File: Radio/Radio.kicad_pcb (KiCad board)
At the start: 2 copper layers, 65 x 125.5 mm, 34 parts, among them IC1 SI4844-A10-GU, J1 AudioJack3, J2 Conn_01x04_Pin, J3 AM_ANTENNA_CONNECTOR, Q1 NPN, U1 ARDUINO_PRO_MINI, Y1 32.768 kHz

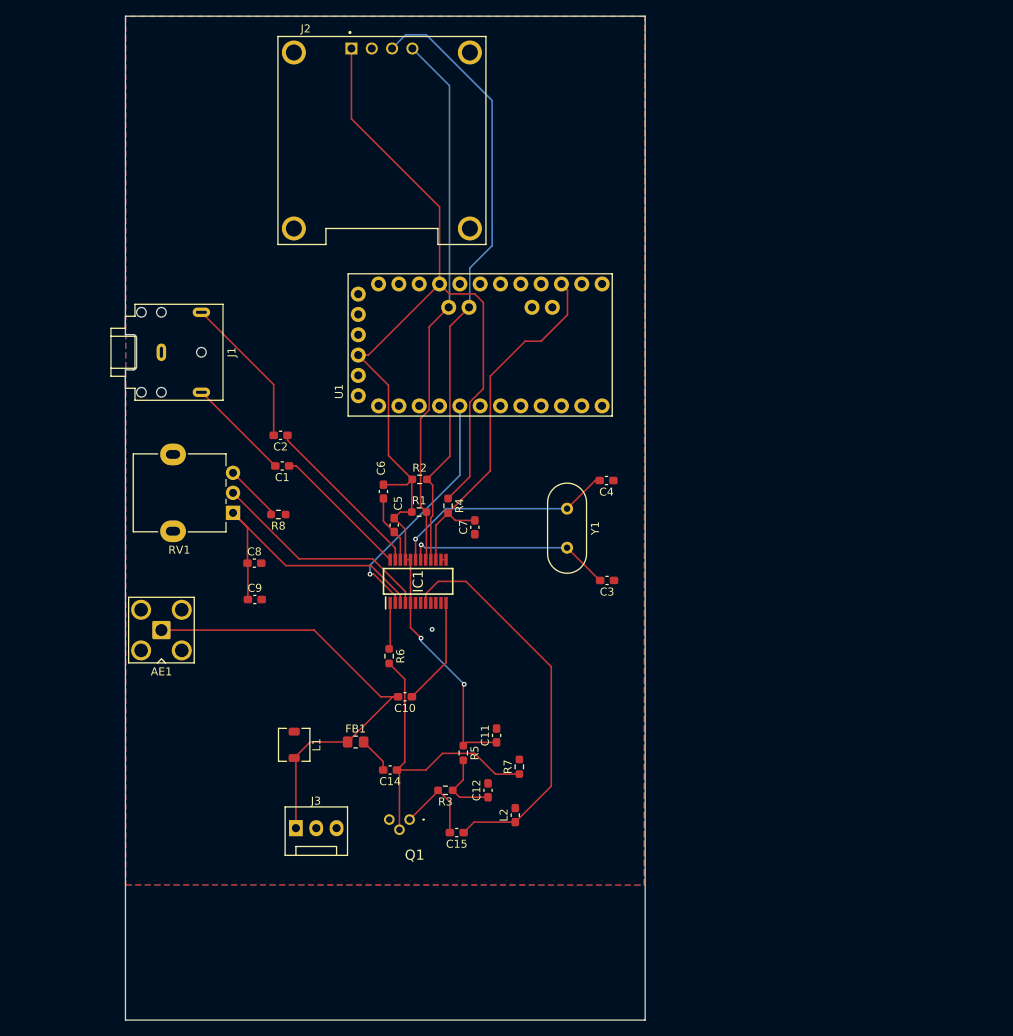
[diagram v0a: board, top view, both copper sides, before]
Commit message: Update PCB: move components
Moved several components to new positions. and changed potentiometer footprint
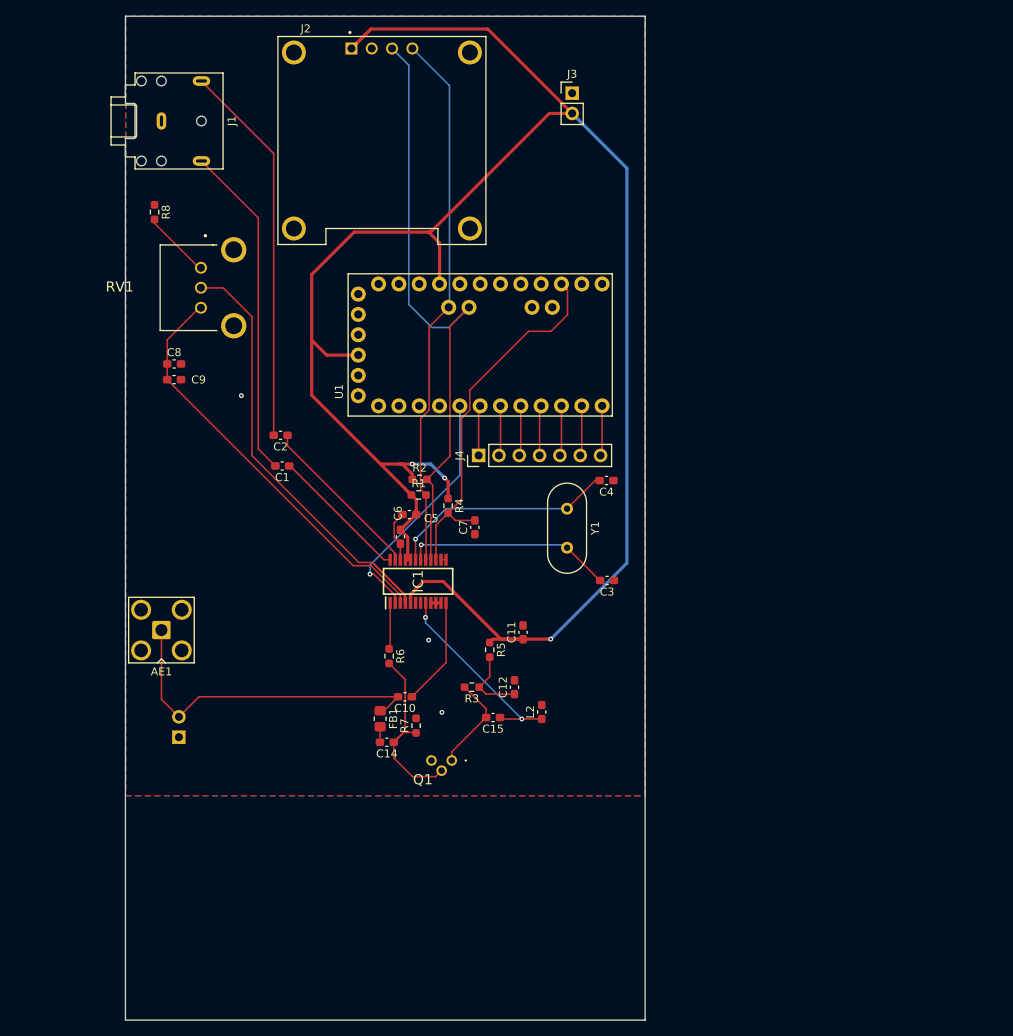
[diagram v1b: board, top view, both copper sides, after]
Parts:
- added J4: Conn_01x07_Pin, Connector_PinHeader_2.54mm:PinHeader_1x07_P2.54mm_Vertical, F.Cu at (115.2, 71.6)
- J3: value AM_ANTENNA_CONNECTOR -> Conn_01x02_Socket; footprint Connector:FanPinHeader_1x03_P2.54mm_Vertical -> Connector_PinHeader_2.54mm:PinHeader_1x02_P2.54mm_Vertical
- L1: value AM_ANT -> L_Ferrite_Small; footprint Inductor_SMD:L_Murata_DEM3518C -> Connector_PinHeader_2.54mm:PinHeader_1x02_P2.54mm_Horizontal; moved to B.Cu
- RV1: footprint Potentiometer_THT:Potentiometer_Alpha_RD901F-40-00D_Single_Vertical -> RadioLib:RK09L1120A2S
- moved J3 98.2 mm to (126.9, 26.4)
- moved R8 40.8 mm to (74.7, 41.2), turned to -90 degrees
- moved RV1 30.9 mm to (80.5, 48.2)
- moved C9 29.3 mm to (77.2, 62.2)
- moved J1 28.9 mm to (75.6, 29.8)
- moved C8 26.8 mm to (77.2, 60.2)
- moved C15 15.1 mm to (117.0, 104.4)
- moved L1 14.4 mm to (77.8, 106.9), turned to 0 degrees
- moved R7 13.9 mm to (107.4, 105.4)
- moved L2 13.3 mm to (123.1, 103.7)
- moved R3 13.3 mm to (114.4, 100.6)
- moved C11 13.3 mm to (120.8, 93.8)
- moved C12 13.3 mm to (119.7, 100.6)
- moved R5 13.3 mm to (116.6, 95.9)
- moved Q1 9.07 mm to (111.9, 109.8)
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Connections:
- J3 pad 1: AM_ANT -> GND
- J3 pad 2: GND -> +3V3
- RV1 pad 1: TUNE1 -> Net-(R8-Pad2)
- RV1 pad 3: Net-(R8-Pad2) -> TUNE1
- U1 pad JP7_1: unconnected-(U1-D9-PadJP7_1) -> ROW1
- U1 pad JP7_2: unconnected-(U1-D8-PadJP7_2) -> ROW2
- U1 pad JP7_3: unconnected-(U1-D7-PadJP7_3) -> ROW3
- U1 pad JP7_4: unconnected-(U1-D6-PadJP7_4) -> ROW4
- U1 pad JP7_5: unconnected-(U1-D5-PadJP7_5) -> COL1
- U1 pad JP7_6: unconnected-(U1-D4-PadJP7_6) -> COL2
- U1 pad JP7_7: unconnected-(U1-D3-PadJP7_7) -> COL3
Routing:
- net +3V3: track 146.3 -> 249.1 mm, vias 2 -> 3
- net TUNE2: track 28.1 -> 59.7 mm
- net Net-(C1-Pad2): track 13.1 -> 42.5 mm
- net Net-(C2-Pad2): track 19.1 -> 48.0 mm
- net FM_ANT: track 50.2 -> 24.8 mm, vias 0 -> 2
- net Net-(Q1-B): track 39.4 -> 23.8 mm
- net AM_ANT: track 58.1 -> 43.6 mm
- net TUNE1: track 38.0 -> 51.9 mm
- net ROW3: track 0.00 -> 6.28 mm
- net COL3: track 0.00 -> 6.28 mm
- net COL1: track 0.00 -> 6.28 mm
- net ROW4: track 0.00 -> 6.28 mm
- net ROW2: track 0.00 -> 6.28 mm
- net COL2: track 0.00 -> 6.28 mm
- net ROW1: track 0.00 -> 6.28 mm
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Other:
- outline, holes or cut-outs redrawn

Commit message: Update PCB layout and footprints
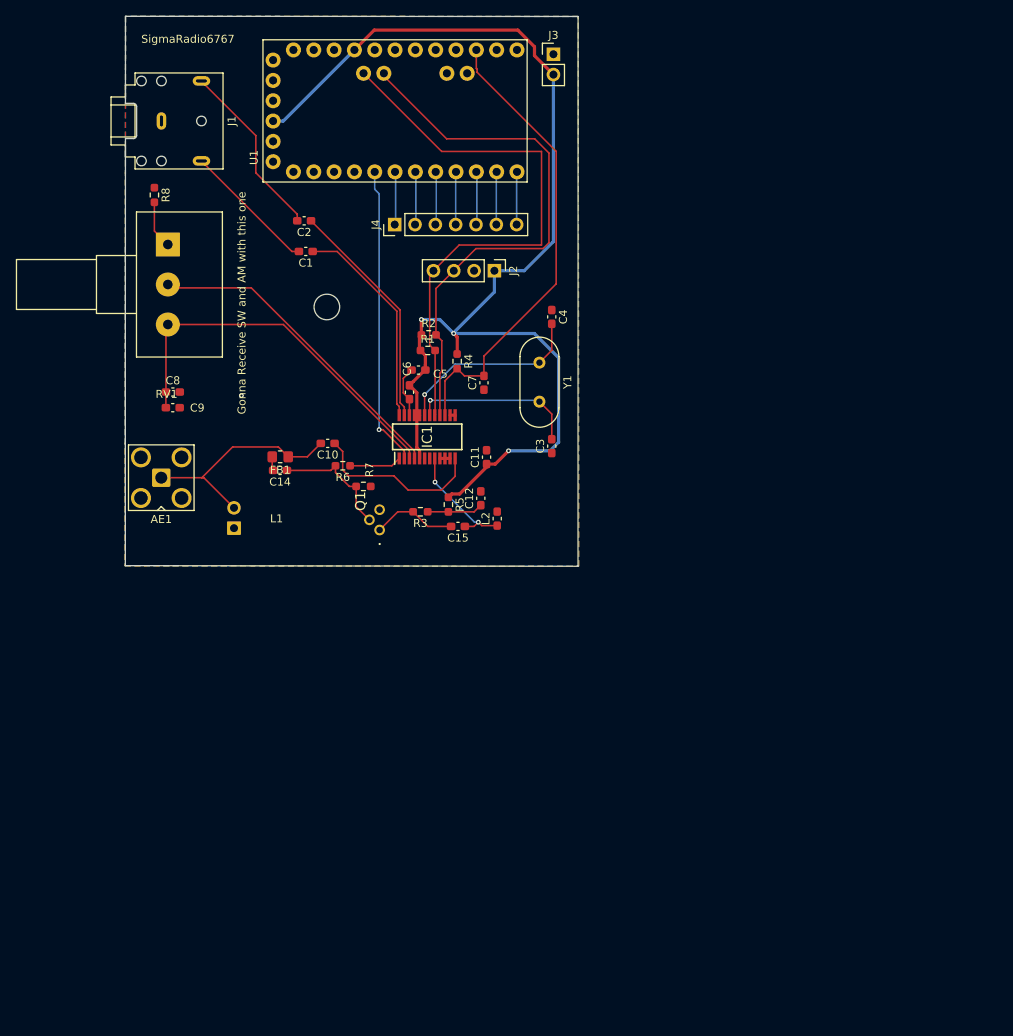
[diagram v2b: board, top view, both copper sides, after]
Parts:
- added REF**: MountingHole_3.2mm_M3_DIN965, MountingHole:MountingHole_3.2mm_M3_DIN965, F.Cu at (96.2, 53.1)
- J2: footprint DM-OLED096-636:MODULE_DM-OLED096-636 -> Connector_PinHeader_2.54mm:PinHeader_1x04_P2.54mm_Vertical
- RV1: footprint RadioLib:RK09L1120A2S -> Potentiometer_THT:Potentiometer_Alps_RK163_Single_Horizontal
- moved C14 36.5 mm to (90.4, 73.5)
- moved FB1 35.0 mm to (90.4, 71.8), turned to 180 degrees
- moved C10 33.1 mm to (96.3, 70.1)
- moved U1 31.1 mm to (104.8, 28.6)
- moved J4 30.7 mm to (104.7, 42.8)
- moved R7 30.6 mm to (100.8, 75.5), turned to 0 degrees
- moved Q1 30.2 mm to (102.8, 81.0), turned to 90 degrees
- moved L1 27.0 mm to (84.6, 80.7)
- moved C1 27.0 mm to (93.6, 46.1)
- moved C2 27.0 mm to (93.4, 42.3)
- moved L2 24.8 mm to (117.5, 79.5)
- moved R6 24.5 mm to (98.2, 72.9), turned to 180 degrees
- moved C15 24.3 mm to (112.6, 80.5)
- moved C12 24.0 mm to (115.5, 77.0)
- moved R3 22.9 mm to (107.9, 78.7)
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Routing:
- net +3V3: track 249.1 -> 152.2 mm
- net Net-(C2-Pad2): track 48.0 -> 22.4 mm
- net Net-(C1-Pad2): track 42.5 -> 17.4 mm
- net TUNE2: track 59.7 -> 40.5 mm
- net AM_ANT: track 43.6 -> 29.1 mm
- net RST: track 47.0 -> 58.8 mm
- net FM_ANT: track 24.8 -> 14.9 mm
- net Net-(IC1-LOUT): track 17.5 -> 26.9 mm
- net Net-(Q1-B): track 23.8 -> 15.3 mm
- net Net-(IC1-AMI): track 13.5 -> 21.8 mm
- net Net-(IC1-ROUT): track 21.1 -> 29.1 mm
- net SDIO: track 76.8 -> 68.9 mm
- net IRQ: track 30.9 -> 37.6 mm
- net XTAL1: track 26.1 -> 20.9 mm
- net XTAL2: track 28.6 -> 24.1 mm
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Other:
- board size 65 x 125.5 mm -> 56.6 x 68.7 mm
- board text added: "Gonna Receive SW and AM with this one"
- board text added: "SigmaRadio6767"

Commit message: Updated PCB
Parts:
- removed C5: 4.7uF, Capacitor_SMD:C_0603_1608Metric_Pad1.08x0.95mm_HandSolder
- removed C6, C7, C9: 0.1uF, Capacitor_SMD:C_0603_1608Metric_Pad1.08x0.95mm_HandSolder
- removed C8: 47uF, Capacitor_SMD:C_0603_1608Metric_Pad1.08x0.95mm_HandSolder
- removed IC1: SI4844-A10-GU, RadioLib:SOP64P600X175-24N
- removed J3: Conn_01x02_Socket, Connector_PinHeader_2.54mm:PinHeader_1x02_P2.54mm_Vertical
- removed J4: Conn_01x07_Pin, Connector_PinHeader_2.54mm:PinHeader_1x07_P2.54mm_Vertical
- removed R1, R2: 2.2K, Resistor_SMD:R_0603_1608Metric_Pad0.98x0.95mm_HandSolder
- removed R4: 100K, Resistor_SMD:R_0603_1608Metric_Pad0.98x0.95mm_HandSolder
- removed R6: 120K, Resistor_SMD:R_0603_1608Metric_Pad0.98x0.95mm_HandSolder
- removed R8: 100, Resistor_SMD:R_0603_1608Metric_Pad0.98x0.95mm_HandSolder
- removed REF**: MountingHole_3.2mm_M3_DIN965, MountingHole:MountingHole_3.2mm_M3_DIN965
- removed RV1: 100K, Potentiometer_THT:Potentiometer_Alps_RK163_Single_Horizontal
- added C19: 22nF, Capacitor_SMD:C_0603_1608Metric_Pad1.08x0.95mm_HandSolder, F.Cu at (148.7, 50.5)
- added C20: 100nF, Capacitor_SMD:C_0603_1608Metric_Pad1.08x0.95mm_HandSolder, F.Cu at (148.8, 52.0)
- added D1: 1N4148, Diode_THT:D_DO-35_SOD27_P7.62mm_Horizontal, F.Cu at (163.4, 79.2)
- added D2: 1N4148, Diode_THT:D_DO-35_SOD27_P7.62mm_Horizontal, F.Cu at (154.9, 79.2)
- added D3: 1N4148, Diode_THT:D_DO-35_SOD27_P7.62mm_Horizontal, F.Cu at (172.0, 79.2)
- added D4: 1N4148, Diode_THT:D_DO-35_SOD27_P7.62mm_Horizontal, F.Cu at (152.1, 76.1)
- added R11: 1k, Resistor_SMD:R_0603_1608Metric_Pad0.98x0.95mm_HandSolder, F.Cu at (149.8, 45.9)
- added R12: 1k, Resistor_SMD:R_0603_1608Metric_Pad0.98x0.95mm_HandSolder, F.Cu at (148.1, 45.9)
- added SW1: RotaryEncoder_Switch, Rotary_Encoder:RotaryEncoder_Alps_EC11E-Switch_Vertical_H20mm_CircularMountingHoles, F.Cu at (171.6, 60.5)
- added SW2: SW_Push_45deg, FSM8JH:SW_FSM8JH, F.Cu at (165.6, 92.9)
- added SW3: SW_Push_45deg, FSM8JH:SW_FSM8JH, F.Cu at (174.1, 92.9)
- added SW4: SW_Push_45deg, FSM8JH:SW_FSM8JH, F.Cu at (157.1, 92.9)
- added U2: RP2040-ZERO, RP2040-ZERO:MODULE_RP2040-ZERO, F.Cu at (167.2, 45.1)
- added U5: PAM8301, Package_TO_SOT_SMD:SOT-23-6_Handsoldering, F.Cu at (146.3, 40.6)
- C1: value 4.7uF -> 10uF
- C2: value 4.7uF -> 0.1uF
- J2: footprint Connector_PinHeader_2.54mm:PinHeader_1x04_P2.54mm_Vertical -> DM-OLED096-636:MODULE_DM-OLED096-636
- L1: moved to F.Cu
- U1: value ARDUINO_PRO_MINI -> Si4735-D60-GU; footprint ARDUINO_PRO_MINI:MODULE_ARDUINO_PRO_MINI -> Package_SO:SSOP-24_3.9x8.7mm_P0.635mm
- moved J1 61.5 mm to (136.6, 37.8), turned to 180 degrees
- moved AE1 61.0 mm to (124.4, 37.8), turned to 0 degrees
- moved C1 55.9 mm to (148.7, 36.5), turned to 90 degrees
- moved C2 53.3 mm to (146.3, 36.5), turned to -90 degrees
- moved L1 50.7 mm to (130.4, 58.8), turned to 180 degrees
- moved U1 45.5 mm to (143.3, 52.8), turned to 0 degrees
- moved FB1 43.9 mm to (124.4, 44.1), turned to -90 degrees
- moved C10 43.5 mm to (137.8, 57.0)
- moved C14 42.7 mm to (124.4, 47.6), turned to 90 degrees
- moved Q1 39.5 mm to (128.4, 50.9)
- moved J2 39.5 mm to (136.1, 83.2), turned to 0 degrees
- moved R3 38.5 mm to (132.6, 49.1)
- moved R5 38.0 mm to (135.3, 48.2)
- moved C15 36.9 mm to (136.6, 52.5)
- moved C12 34.2 mm to (132.6, 47.4), turned to 180 degrees
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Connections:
- C1 pad 1: Net-(IC1-LOUT) -> +3V3
- C1 pad 2: Net-(C1-Pad2) -> GND
- C10 pad 1: Net-(IC1-AMI) -> AM_ANT_IC
- C2 pad 1: Net-(IC1-ROUT) -> GND
- C2 pad 2: Net-(C2-Pad2) -> +3V3
- J1 pad R: Net-(C2-Pad2) -> Net-(U5-OUT-)
- J1 pad T: Net-(C1-Pad2) -> Net-(U5-OUT+)
- J2 pad 3: SDIO -> SDA_OLED
- J2 pad 4: SCLK -> SCLK_OLED
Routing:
- net SDIO: track 68.9 -> 0.00 mm
- net +3V3: track 152.2 -> 91.7 mm, vias 3 -> 2
- net SCLK: track 71.5 -> 14.3 mm
- net TUNE1: track 48.2 -> 0.00 mm
- net ROW1: track 6.66 -> 52.4 mm
- net TUNE2: track 40.5 -> 0.00 mm
- net ROW2: track 6.50 -> 44.7 mm
- net IRQ: track 37.6 -> 0.00 mm, vias 1 -> 0
- net RST: track 58.8 -> 21.2 mm
- net SDA_OLED: track 0.00 -> 36.7 mm
- net COL1: track 6.66 -> 41.7 mm, vias 0 -> 1
- net SCLK_OLED: track 0.00 -> 32.1 mm
- net COL2: track 6.66 -> 35.9 mm
- net Net-(IC1-ROUT): track 29.1 -> 0.00 mm
- net Net-(IC1-LOUT): track 26.9 -> 0.00 mm
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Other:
- board size 56.6 x 68.7 mm -> 62.8 x 64.1 mm
- board text removed: "Gonna Receive SW and AM with this one"
- board text removed: "SigmaRadio6767"

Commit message: push to git
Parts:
- removed C12: 33nF, Capacitor_SMD:C_0603_1608Metric_Pad1.08x0.95mm_HandSolder
- removed C15: 10pF, Capacitor_SMD:C_0603_1608Metric_Pad1.08x0.95mm_HandSolder
- removed Q1: NPN, RadioLib:SS9018
- removed R11, R12: 1k, Resistor_SMD:R_0603_1608Metric_Pad0.98x0.95mm_HandSolder
- removed R3: 1K, Resistor_SMD:R_0603_1608Metric_Pad0.98x0.95mm_HandSolder
- removed R5: 10, Resistor_SMD:R_0603_1608Metric_Pad0.98x0.95mm_HandSolder
- removed R7: 100K, Resistor_SMD:R_0603_1608Metric_Pad0.98x0.95mm_HandSolder
- added C5: 1uF, Capacitor_SMD:C_0603_1608Metric_Pad1.08x0.95mm_HandSolder, F.Cu at (111.3, 52.0)
- added C6: 1uF, Capacitor_SMD:C_0603_1608Metric_Pad1.08x0.95mm_HandSolder, F.Cu at (111.1, 54.1)
- added C7: 0.1uF, Capacitor_SMD:C_0603_1608Metric_Pad1.08x0.95mm_HandSolder, F.Cu at (140.6, 48.3)
- added C8: 0.39uF, Capacitor_SMD:C_0603_1608Metric_Pad1.08x0.95mm_HandSolder, F.Cu at (128.0, 53.3)
- added C9: 0.39uF, Capacitor_SMD:C_0603_1608Metric_Pad1.08x0.95mm_HandSolder, F.Cu at (127.9, 55.1)
- added D5: CM1213A-01SO, Package_TO_SOT_SMD:SOT-23, F.Cu at (91.3, 69.8)
- added D6: CM1213A-01SO, Package_TO_SOT_SMD:SOT-23, F.Cu at (93.3, 64.0)
- added FB2: 1k, Resistor_SMD:R_0805_2012Metric_Pad1.20x1.40mm_HandSolder, F.Cu at (113.6, 63.4)
- added J3: AudioJack3, Connector_Audio:Jack_3.5mm_CUI_SJ1-3523N_Horizontal, F.Cu at (120.5, 37.8)
- added L3: 4.7uH, Inductor_SMD:L_0603_1608Metric_Pad1.05x0.95mm_HandSolder, F.Cu at (87.1, 70.7)
- added R1: 100, Resistor_SMD:R_0603_1608Metric_Pad0.98x0.95mm_HandSolder, F.Cu at (114.7, 52.0)
- added R2: 100, Resistor_SMD:R_0603_1608Metric_Pad0.98x0.95mm_HandSolder, F.Cu at (114.5, 54.2)
- added R4: 20k, Resistor_SMD:R_0603_1608Metric_Pad0.98x0.95mm_HandSolder, F.Cu at (131.3, 53.3)
- added R6: 20k, Resistor_SMD:R_0603_1608Metric_Pad0.98x0.95mm_HandSolder, F.Cu at (131.3, 55.0)
- added R8: 20k, Resistor_SMD:R_0603_1608Metric_Pad0.98x0.95mm_HandSolder, F.Cu at (141.0, 50.8)
- added R9: 20k, Resistor_SMD:R_0603_1608Metric_Pad0.98x0.95mm_HandSolder, F.Cu at (134.3, 50.5)
- added U3: PAM8302AAY, Package_DFN_QFN:DFN-8-1EP_3x3mm_P0.65mm_EP1.55x2.4mm, F.Cu at (120.7, 51.1)
- added U4: LM4910MM, LM4910MM:SOP65P490X110-8N, F.Cu at (136.9, 50.5)
- C11: value 0.47uF -> 33pF
- C14: value 33nF -> 18pF
- L1: footprint Connector_PinHeader_2.54mm:PinHeader_1x02_P2.54mm_Horizontal -> Connector_PinHeader_2.54mm:PinHeader_1x02_P2.54mm_Vertical
- L2: value 270nH -> 180nH
- U5: value PAM8301 -> PE4259; footprint Package_TO_SOT_SMD:SOT-23-6_Handsoldering -> PE4259:SOT65P215X110-6N
- Y1: footprint Crystal:Crystal_HC49-4H_Vertical -> Crystal:Crystal_SMD_0603-2Pin_6.0x3.5mm_HandSoldering
- moved U5 67.9 mm to (83.5, 66.3), turned to -90 degrees
- moved C11 57.9 mm to (83.6, 70.7), turned to 0 degrees
- moved L1 54.9 mm to (77.5, 73.2)
- moved AE1 44.5 mm to (79.9, 37.8)
- moved C3 42.8 mm to (110.1, 73.4)
- moved C19 41.9 mm to (108.9, 63.4)
- moved U1 41.9 mm to (103.5, 65.6)
- moved C10 41.9 mm to (98.0, 69.8)
- moved L2 41.9 mm to (96.8, 67.0)
- moved C20 41.9 mm to (108.9, 64.9)
- moved C4 40.4 mm to (96.8, 73.4)
- moved FB1 40.4 mm to (88.0, 61.5)
- moved C14 39.3 mm to (88.7, 64.1), turned to 180 degrees
- moved Y1 39.0 mm to (103.4, 73.2)
- moved C1 4.07 mm to (152.8, 36.5)
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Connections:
- AE1 pad 1: AM_ANT -> /SW
- C10 pad 2: AM_ANT -> Net-(D5-VN)
- C11 pad 1: +3V3 -> /AM
- C11 pad 2: GND -> /Common
- C19 pad 2: +3V3 -> /RF_PWR
- C20 pad 1: +3V3 -> /RF_PWR
- FB1 pad 1: AM_ANT -> /SW
- J1 pad R: Net-(U5-OUT-) -> /OUT_R
- J1 pad S: GND -> Net-(U4-VO3)
- J1 pad T: Net-(U5-OUT+) -> /OUT_T
- L1 pad 2: AM_ANT -> /AM
- U1 pad 20: +3V3 -> /RF_PWR
- U1 pad 21: +3V3 -> /RF_PWR
- U1 pad 23: Net-(U1-ROUT/[DOUT]) -> /Audio-
- U1 pad 24: Net-(U1-LOUT/[DFS]) -> /Audio+
- U2 pad 10: COL2 -> Ant_Switch
- U2 pad 19: unconnected-(U2-GP28-Pad19) -> headphone_enable
- U2 pad 20: Aud_Enable -> spk_Enable
- U2 pad 23: unconnected-(U2-5V-Pad23) -> VBUS
- U2 pad 6: unconnected-(U2-GP5-Pad6) -> COL1
- U2 pad 7: COL1 -> ROW1
- U2 pad 8: ROW1 -> ROW2
- U2 pad 9: ROW2 -> COL2
- U5 pad 1: Net-(U5-OUT-) -> /SW
- U5 pad 3: Audio_Amp -> /AM
- U5 pad 4: Aud_Enable -> Ant_Switch
- U5 pad 5: +3V3 -> /Common
- U5 pad 6: Net-(U5-OUT+) -> /RF_PWR
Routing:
- net Ant_Switch: track 0.00 -> 112.9 mm
- net /RF_PWR: track 0.00 -> 89.7 mm, vias 0 -> 2
- net +3V3: track 91.7 -> 142.1 mm, vias 2 -> 3
- net spk_Enable: track 0.00 -> 46.2 mm, vias 0 -> 2
- net SDA: track 13.8 -> 59.2 mm
- net SCLK: track 14.3 -> 58.2 mm
- net Enable: track 18.2 -> 61.0 mm
- net RST: track 21.2 -> 63.8 mm
- net AM_ANT: track 37.8 -> 0.00 mm
- net /Audio+: track 0.00 -> 32.6 mm
- net /SW: track 0.00 -> 32.4 mm
- net /Audio-: track 0.00 -> 29.6 mm
- net headphone_enable: track 0.00 -> 26.7 mm, vias 0 -> 2
- net Net-(U4-VO3): track 0.00 -> 19.5 mm
- net GND: track 9.57 -> 27.8 mm, vias 21 -> 14
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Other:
- board size 62.8 x 64.1 mm -> 110.8 x 64.1 mm
